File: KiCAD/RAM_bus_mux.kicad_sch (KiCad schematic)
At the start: 0 parts

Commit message: fix multiple ERCs that made RAM addrs not connecting
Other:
- sheet 15bit_2:1_MUX ports: added O_[0..14]; removed O[0..14]
- sheet 15bit_2:1_MUX1 ports: added O_[0..14]; removed O[0..14]
- sheet 8bit_2:1_MUX ports: added O_[0..7]; removed O[0..7]
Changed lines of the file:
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@@
+		)
+	)
+	(label "w_addr[0..14]"
+		(at 86.36 85.09 0)
+		(effects
+			(font
+				(size 1.27 1.27)
+			)
+			(justify left bottom)
 		)
 	)
@@
 			)
 			(justify right bottom)
+		)
+	)
+	(label "r_addr[0..14]"
+		(at 86.36 71.12 0)
+		(effects
+			(font
+				(size 1.27 1.27)
+			)
+			(justify left bottom)
 		)
 	)
@@
 			)
 		)
-		(pin "O[0..14]" output
+		(pin "O_[0..14]" output
 			(at 138.43 93.98 0)
 			(effects
@@
 			)
 		)
-		(pin "O[0..7]" output
+		(pin "O_[0..7]" output
 			(at 248.92 92.71 0)
 			(effects
@@
 			)
 		)
-		(pin "O[0..14]" output
+		(pin "O_[0..14]" output
 			(at 138.43 66.04 0)
 			(effects

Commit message: resolve ERCs for addr combiner
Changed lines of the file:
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@@
-		)
-	)
-	(label "w_addr[0..14]"
-		(at 86.36 85.09 0)
-		(effects
-			(font
-				(size 1.27 1.27)
-			)
-			(justify left bottom)
 		)
 	)
@@
 		)
 	)
-	(label "r_addr[0..14]"
-		(at 86.36 71.12 0)
-		(effects
-			(font
-				(size 1.27 1.27)
-			)
-			(justify left bottom)
-		)
-	)

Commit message: clean up; resolve ERC warnings
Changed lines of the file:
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@@
 		(color 0 0 0 0)
 	)
-	(junction
-		(at 104.14 85.09)
-		(diameter 0)
-		(color 0 0 0 0)
-	)
-	(junction
-		(at 106.68 71.12)
-		(diameter 0)
-		(color 0 0 0 0)
+	(bus
+		(pts
+			(xy 113.03 101.6) (xy 115.57 101.6)
+		)
+		(stroke
+			(width 0)
+			(type default)
+		)
+	)
+	(bus
+		(pts
+			(xy 114.3 73.66) (xy 115.57 73.66)
+		)
+		(stroke
+			(width 0)
+			(type default)
+		)
 	)
 	(bus
@@
 	(bus
 		(pts
-			(xy 115.57 71.12) (xy 106.68 71.12)
-		)
-		(stroke
-			(width 0)
-			(type default)
-		)
-	)
-	(bus
-		(pts
 			(xy 262.89 82.55) (xy 210.82 82.55)
 		)
@@
 		)
 	)
-	(bus
-		(pts
-			(xy 83.82 71.12) (xy 106.68 71.12)
-		)
-		(stroke
-			(width 0)
-			(type default)
-		)
-	)
 	(wire
 		(pts
@@
 	(bus
 		(pts
+			(xy 83.82 71.12) (xy 85.09 71.12)
+		)
+		(stroke
+			(width 0)
+			(type default)
+		)
+	)
+	(bus
+		(pts
 			(xy 213.36 97.79) (xy 226.06 97.79)
 		)
@@
 	(bus
 		(pts
-			(xy 104.14 99.06) (xy 115.57 99.06)
-		)
-		(stroke
-			(width 0)
-			(type default)
-		)
-	)
-	(bus
-		(pts
 			(xy 248.92 92.71) (xy 261.62 92.71)
 		)
@@
 	(bus
 		(pts
-			(xy 104.14 85.09) (xy 104.14 99.06)
-		)
-		(stroke
-			(width 0)
-			(type default)
-		)
-	)
-	(bus
-		(pts
 			(xy 210.82 100.33) (xy 226.06 100.33)
 		)
@@
 	(bus
 		(pts
-			(xy 106.68 101.6) (xy 115.57 101.6)
-		)
-		(stroke
-			(width 0)
-			(type default)
-		)
-	)
-	(bus
-		(pts
 			(xy 213.36 97.79) (xy 213.36 85.09)
 		)
@@
 	(bus
 		(pts
-			(xy 104.14 73.66) (xy 104.14 85.09)
-		)
-		(stroke
-			(width 0)
-			(type default)
-		)
-	)
-	(bus
-		(pts
 			(xy 43.18 68.58) (xy 54.61 68.58)
 		)
@@
 	(bus
 		(pts
-			(xy 106.68 71.12) (xy 106.68 101.6)
-		)
-		(stroke
-			(width 0)
-			(type default)
-		)
-	)
-	(bus
-		(pts
 			(xy 265.43 85.09) (xy 265.43 68.58)
 		)
@@
 	(bus
 		(pts
-			(xy 115.57 73.66) (xy 104.14 73.66)
-		)
-		(stroke
-			(width 0)
-			(type default)
-		)
-	)
-	(bus
-		(pts
-			(xy 83.82 85.09) (xy 104.14 85.09)
+			(xy 113.03 99.06) (xy 115.57 99.06)
+		)
+		(stroke
+			(width 0)
+			(type default)
+		)
+	)
+	(bus
+		(pts
+			(xy 114.3 71.12) (xy 115.57 71.12)
+		)
+		(stroke
+			(width 0)
+			(type default)
+		)
+	)
+	(bus
+		(pts
+			(xy 83.82 85.09) (xy 85.09 85.09)
 		)
 		(stroke
@@
 		)
 	)
+	(label "w_addr[0..14]"
+		(at 85.09 85.09 0)
+		(effects
+			(font
+				(size 1.27 1.27)
+			)
+			(justify left bottom)
+		)
+	)
+	(label "w_addr[0..14]"
+		(at 114.3 73.66 180)
+		(effects
+			(font
+				(size 1.27 1.27)
+			)
+			(justify right bottom)
+		)
+	)
 	(label "rbit_0"
 		(at 224.79 92.71 180)
@@
 		)
 	)
+	(label "r_addr[0..14]"
+		(at 114.3 71.12 180)
+		(effects
+			(font
+				(size 1.27 1.27)
+			)
+			(justify right bottom)
+		)
+	)
+	(label "r_addr[0..14]"
+		(at 113.03 101.6 180)
+		(effects
+			(font
+				(size 1.27 1.27)
+			)
+			(justify right bottom)
+		)
+	)
 	(label "rbit_0"
 		(at 86.36 68.58 0)
@@
 		)
 	)
+	(label "r_addr[0..14]"
+		(at 85.09 71.12 0)
+		(effects
+			(font
+				(size 1.27 1.27)
+			)
+			(justify left bottom)
+		)
+	)
 	(label "rbit_0"
 		(at 114.3 66.04 180)
 		(effects
 			(font
+				(size 1.27 1.27)
+			)
+			(justify right bottom)
+		)
+	)
+	(label "w_addr[0..14]"
+		(at 113.03 99.06 180)
+		(effects
+			(font

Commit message: resolved most ERC errors
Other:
- sheet addr_combiner ports: added j_addr0; removed bit0
- sheet addr_combiner1 ports: added j_addr0; removed bit0
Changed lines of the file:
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@@
 			)
 		)
-		(pin "bit0" output
+		(pin "j_addr0" output
 			(at 83.82 68.58 0)
 			(effects
@@
 			)
 		)
-		(pin "bit0" output
+		(pin "j_addr0" output
 			(at 83.82 82.55 0)
 			(effects

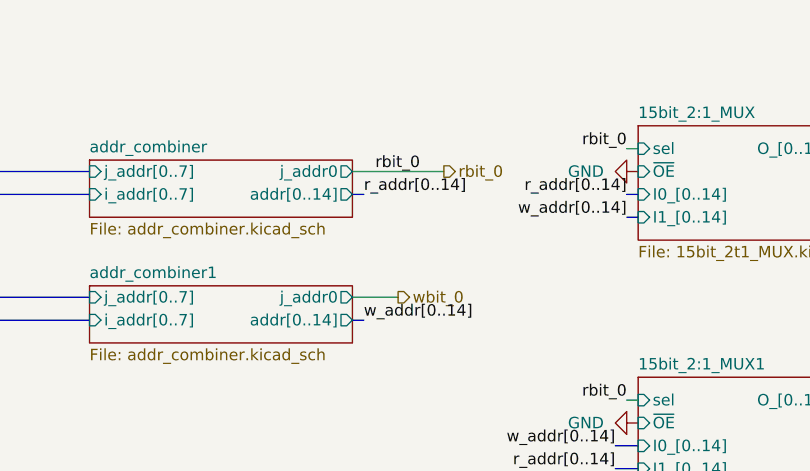
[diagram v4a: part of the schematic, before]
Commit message: resolved all ERC errors, kicad got some stupid bugs
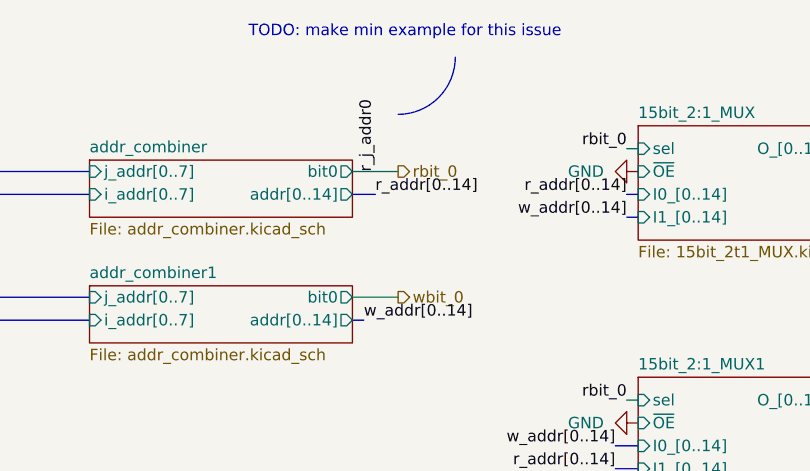
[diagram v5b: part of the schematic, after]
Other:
- sheet addr_combiner ports: added bit0; removed j_addr0
- sheet addr_combiner1 ports: added bit0; removed j_addr0
- note added: "TODO: make min example for this issue"
